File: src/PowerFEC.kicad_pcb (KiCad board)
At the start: 2 copper layers, 24 x 27.9 mm, 14 parts, among them J1 B2B-XH-A, P1 105444-0001, U1 AP22652

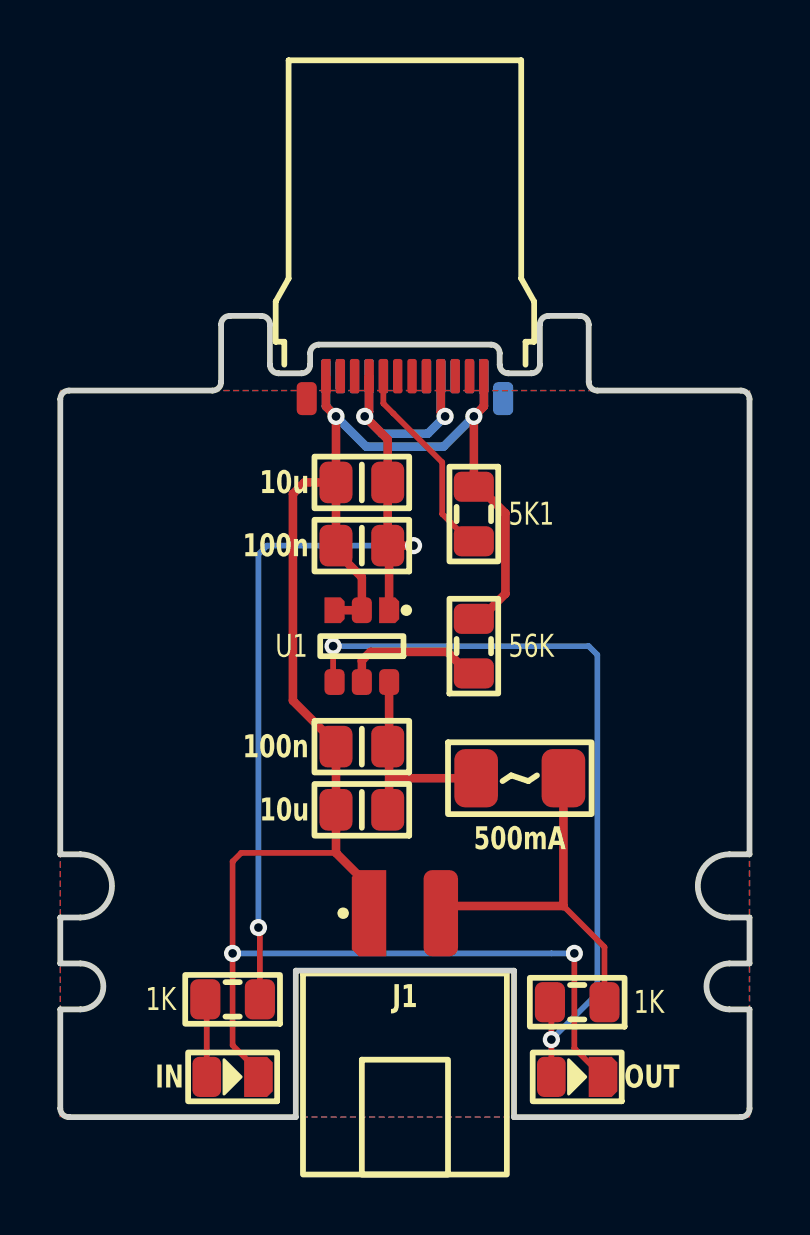
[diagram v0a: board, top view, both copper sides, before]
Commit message: Refactored to allow usage of PIC
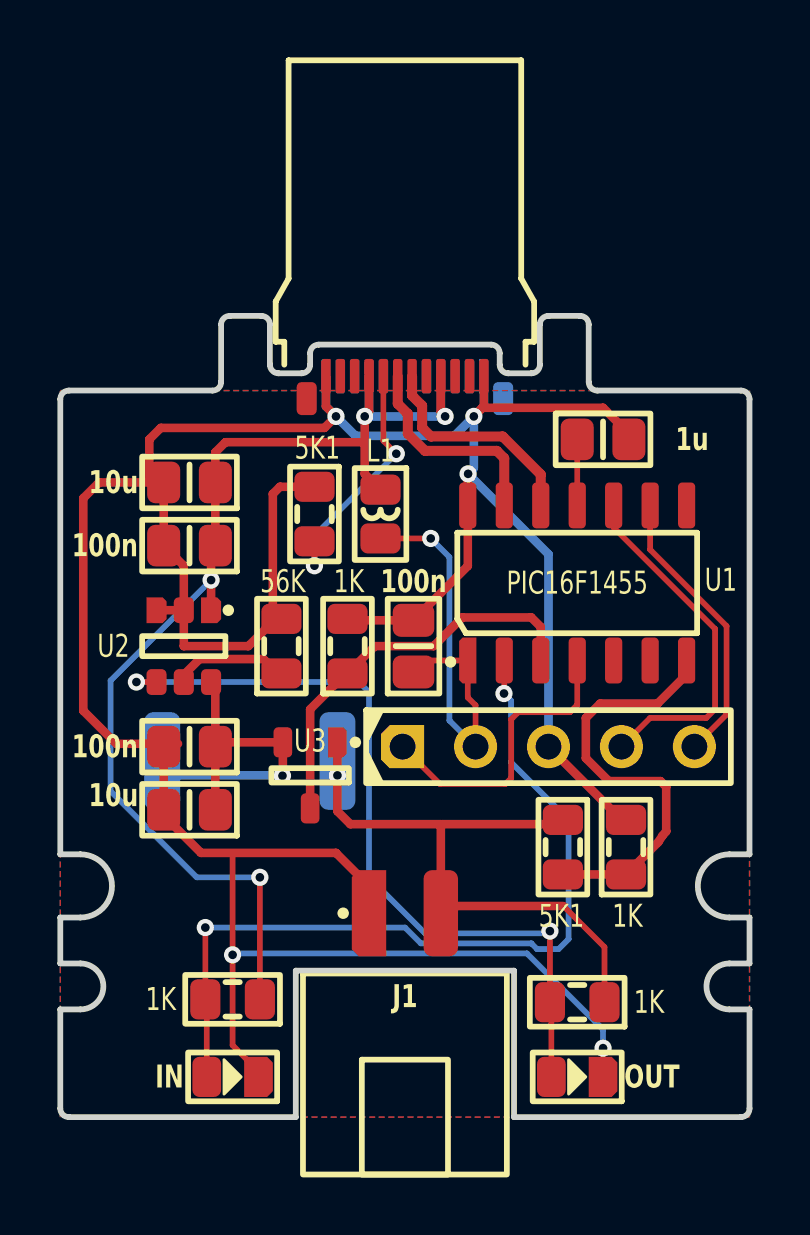
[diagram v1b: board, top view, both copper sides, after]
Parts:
- removed F?: 500mA, Medo64:F (1206)
- added C3: 100n, Medo64:C (0805), F.Cu at (32.3, 31.5)
- added C4: 1u, Medo64:C (0805), F.Cu at (38.9, 24.3)
- added ICSP: Microchip PIC, Medo64:ICSP PIC Pogo (5w), F.Cu at (37.0, 35.0)
- added L1: 1u, Medo64:L (0805), F.Cu at (31.1, 26.9)
- added R1: 0R1, Medo64:R (2512), B.Cu at (26.6, 35.5)
- added R2: 1K, Medo64:R (0805), F.Cu at (30.0, 31.5)
- added R4: 1K, Medo64:R (0805), F.Cu at (39.7, 38.5)
- added R5: 5K1, Medo64:R (0805), F.Cu at (37.5, 38.5)
- added U1: PIC16F1455, Medo64:U Micro PIC16F1455 (SOIC-14), F.Cu at (38.0, 29.3)
- added U3: ZXCT1009, Medo64:U CurrentSense ZXCT1009 (SOT23-3), F.Cu at (28.7, 36.0)
- moved R7 6.70 mm to (27.7, 31.5)
- moved U2 6.20 mm to (24.3, 31.5)
- moved C1 6.00 mm to (24.5, 28.0)
- moved C2 6.00 mm to (24.5, 35.0)
- moved C5 6.00 mm to (24.5, 25.8)
- moved C6 6.00 mm to (24.5, 37.2)
- moved R6 5.55 mm to (28.9, 26.9)
- renumbered C3 to C5, C4 to C6, R1 to R3, R2 to R4, R3 to R6, R4 to R7, U1 to U2
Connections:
- net FAULT# renamed LED_OUT
- net USB_Vin renamed Vin
- C2 pad 1: Vout -> Vsw
- C6 pad 1: Vout -> Vsw
- J1 pad 2: Vfused -> Vout
- R4 pad 1: Vfused -> Vout
- U2 pad 6: Vout -> Vsw
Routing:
- net GND: track 73.7 -> 117.9 mm, vias 4 -> 5
- net LED_IN: track 2.72 -> 28.9 mm, vias 0 -> 2
- net Vout: track 7.54 -> 22.7 mm, vias 0 -> 1
- net Vadc: track 0.00 -> 14.6 mm
- net 5V: track 0.00 -> 14.4 mm, vias 0 -> 1
- net Iadc: track 0.00 -> 14.1 mm
- net Vfused: track 12.9 -> 0.00 mm
- net ICSP_DAT: track 0.00 -> 12.4 mm
- net Vsw: track 0.00 -> 11.9 mm, vias 0 -> 1
- net ICSP_VPP: track 0.00 -> 10.5 mm
- net ICSP_CLK: track 0.00 -> 9.97 mm
- net USB_DM: track 0.00 -> 7.82 mm
- net USB_DP: track 0.00 -> 7.50 mm
- net Vin: track 38.3 -> 43.2 mm
- net V33: track 0.00 -> 2.30 mm
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
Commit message: Refactoring copper pours
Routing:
- net GND: track 117.9 -> 136.0 mm, vias 5 -> 6
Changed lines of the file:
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@@
   (segment (start 29.2 23.9) (end 23.5 23.9) (width 0.3) (layer "F.Cu") (net 4))
   (via (at 26 42.25) (size 0.6) (drill 0.3) (layers "F.Cu" "B.Cu") (net 4))
+  (via (at 35.5 39.1) (size 0.6) (drill 0.3) (layers "F.Cu" "B.Cu") (net 4))
   (via (at 34.2 25.5) (size 0.6) (drill 0.3) (layers "F.Cu" "B.Cu") (net 4))
   (via (at 29.6 23.5) (size 0.6) (drill 0.3) (layers "F.Cu" "B.Cu") (net 4))
@@
   (via (at 38.9 45.499992) (size 0.6) (drill 0.3) (layers "F.Cu" "B.Cu") (net 4))
   (segment (start 38.9 45.499992) (end 38.9 44.85) (width 0.2) (layer "B.Cu") (net 4))
+  (segment (start 34.2 25.5) (end 32.8 25.5) (width 0.3) (layer "B.Cu") (net 4))
   (segment (start 36.25 42.2) (end 26.05 42.2) (width 0.2) (layer "B.Cu") (net 4))
   (segment (start 26.05 42.2) (end 26 42.25) (width 0.2) (layer "B.Cu") (net 4))
+  (segment (start 33.2 34.2) (end 33.2 36.8) (width 0.3) (layer "B.Cu") (net 4))
   (segment (start 34.4 23.5) (end 34.4 25.3) (width 0.3) (layer "B.Cu") (net 4))
   (segment (start 34.75 23.15) (end 34.4 23.5) (width 0.3) (layer "B.Cu") (net 4))
+  (segment (start 32.8 25.5) (end 30.4 27.9) (width 0.3) (layer "B.Cu") (net 4))
   (segment (start 34.4 25.3) (end 34.2 25.5) (width 0.3) (layer "B.Cu") (net 4))
   (segment (start 29.25 23.15) (end 29.6 23.5) (width 0.3) (layer "B.Cu") (net 4))
@@
   (segment (start 33.724265 24.175735) (end 34.4 23.5) (width 0.3) (layer "B.Cu") (net 4))
   (segment (start 29.25 22.1) (end 29.25 23.15) (width 0.3) (layer "B.Cu") (net 4))
+  (segment (start 30.4 27.9) (end 30.4 31.4) (width 0.3) (layer "B.Cu") (net 4))
+  (segment (start 33.2 36.8) (end 35.5 39.1) (width 0.3) (layer "B.Cu") (net 4))
   (segment (start 29.6 23.5) (end 30.275735 24.175735) (width 0.3) (layer "B.Cu") (net 4))
   (segment (start 37 28.3) (end 34.2 25.5) (width 0.3) (layer "B.Cu") (net 4))
+  (segment (start 30.4 31.4) (end 33.2 34.2) (width 0.3) (layer "B.Cu") (net 4))
   (segment (start 30.1 37.7) (end 29.65 37.25) (width 0.3) (layer "F.Cu") (net 5))
   (segment (start 33.25 40.8) (end 33.25 37.7) (width 0.3) (layer "F.Cu") (net 5))
@@
   (segment (start 31.15 27.75) (end 32.9 27.75) (width 0.2) (layer "F.Cu") (net 8))
   (via (at 32.9 27.75) (size 0.6) (drill 0.3) (layers "F.Cu" "B.Cu") (net 8))
-  (segment (start 33.55 34.09) (end 34.46 35) (width 0.2) (layer "B.Cu") (net 8))
+  (segment (start 34.46 33.56) (end 34.46 35) (width 0.2) (layer "B.Cu") (net 8))
   (segment (start 32.9 27.75) (end 33.55 28.4) (width 0.2) (layer "B.Cu") (net 8))
-  (segment (start 33.55 28.4) (end 33.55 34.09) (width 0.2) (layer "B.Cu") (net 8))
+  (segment (start 33.55 28.4) (end 33.55 32.65) (width 0.2) (layer "B.Cu") (net 8))
+  (segment (start 33.55 32.65) (end 34.46 33.56) (width 0.2) (layer "B.Cu") (net 8))
   (segment (start 38 33.55) (end 38 32) (width 0.2) (layer "F.Cu") (net 9))
   (segment (start 35.7 36.1) (end 35.7 34.05) (width 0.2) (layer "F.Cu") (net 9))
@@
   (segment (start 27.722182 36) (end 23.55 36) (width 0.3) (layer "B.Cu") (net 17))
   (zone (net 4) (net_name "GND") (layers "F&B.Cu") (hatch edge 0.5)
-    (connect_pads (clearance 0.25))
-    (min_thickness 0.25) (filled_areas_thickness no)
+    (connect_pads no (clearance 0.3))
+    (min_thickness 0.3) (filled_areas_thickness no)
     (fill yes (thermal_gap 0.5) (thermal_bridge_width 0.5))
     (polygon

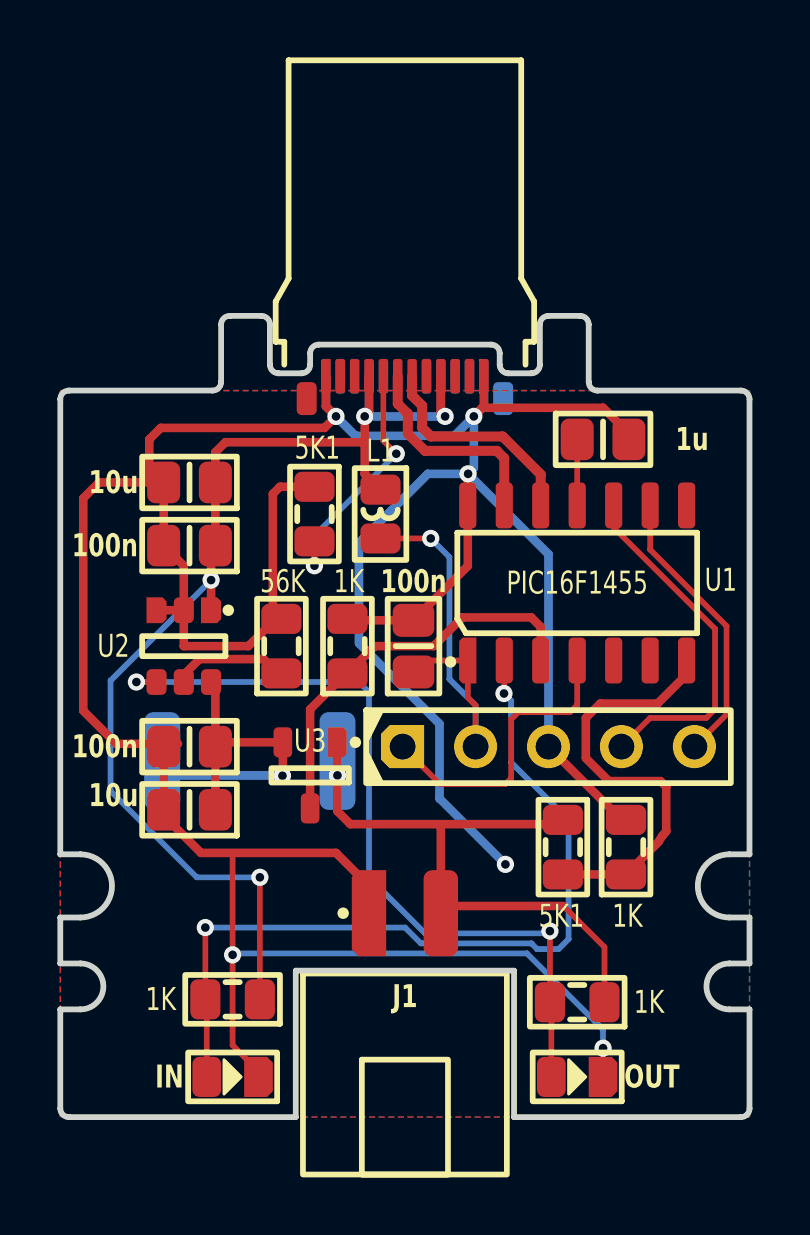
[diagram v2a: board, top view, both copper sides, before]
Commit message: Minor trace movements
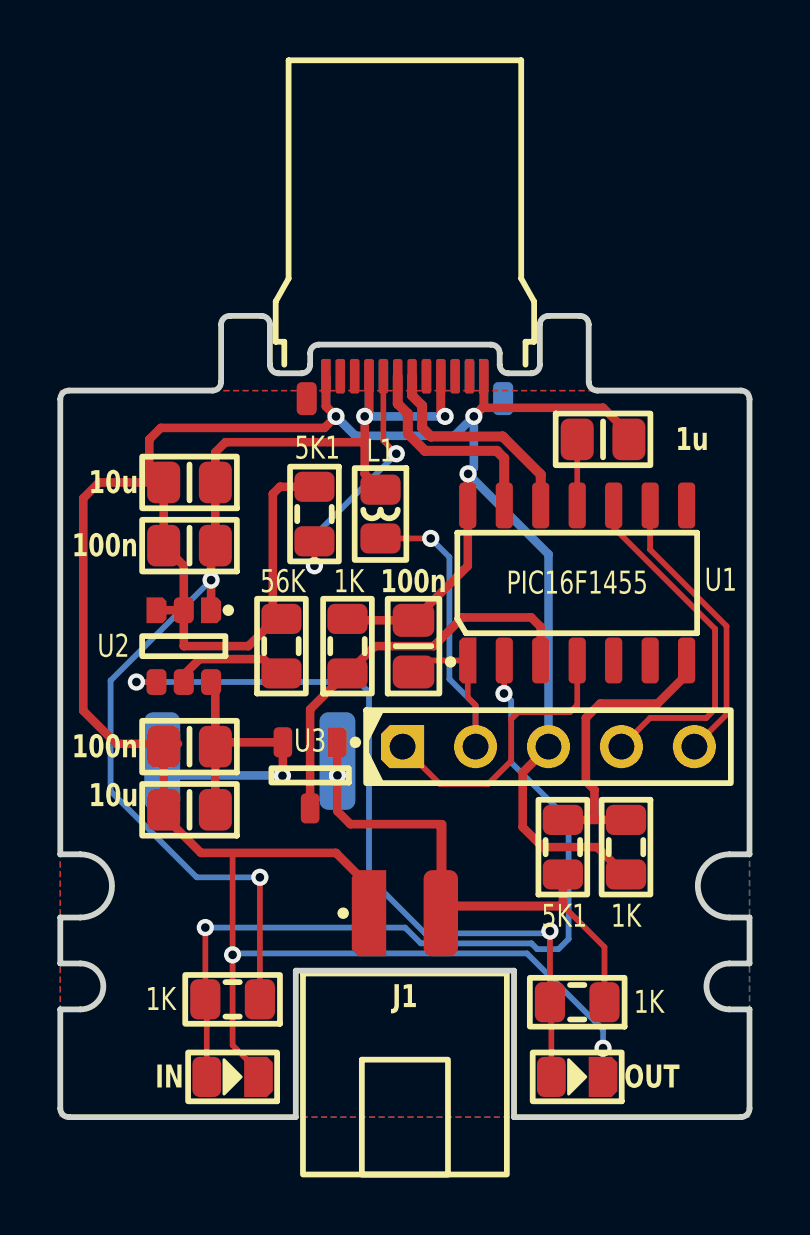
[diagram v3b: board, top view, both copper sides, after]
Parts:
- turned R4 to -90 degrees
- turned R5 to 90 degrees
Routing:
- net GND: track 136.0 -> 121.7 mm, vias 6 -> 5
- net Vadc: track 14.6 -> 10.0 mm
- net Vout: track 22.7 -> 26.8 mm

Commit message: Added soldermask expand
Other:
- rule pad_to_mask_clearance: 0 -> 0.05
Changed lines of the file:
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@@
       (dielectric_constraints no)
     )
-    (pad_to_mask_clearance 0)
+    (pad_to_mask_clearance 0.05)
     (aux_axis_origin 20 20)
     (pcbplotparams

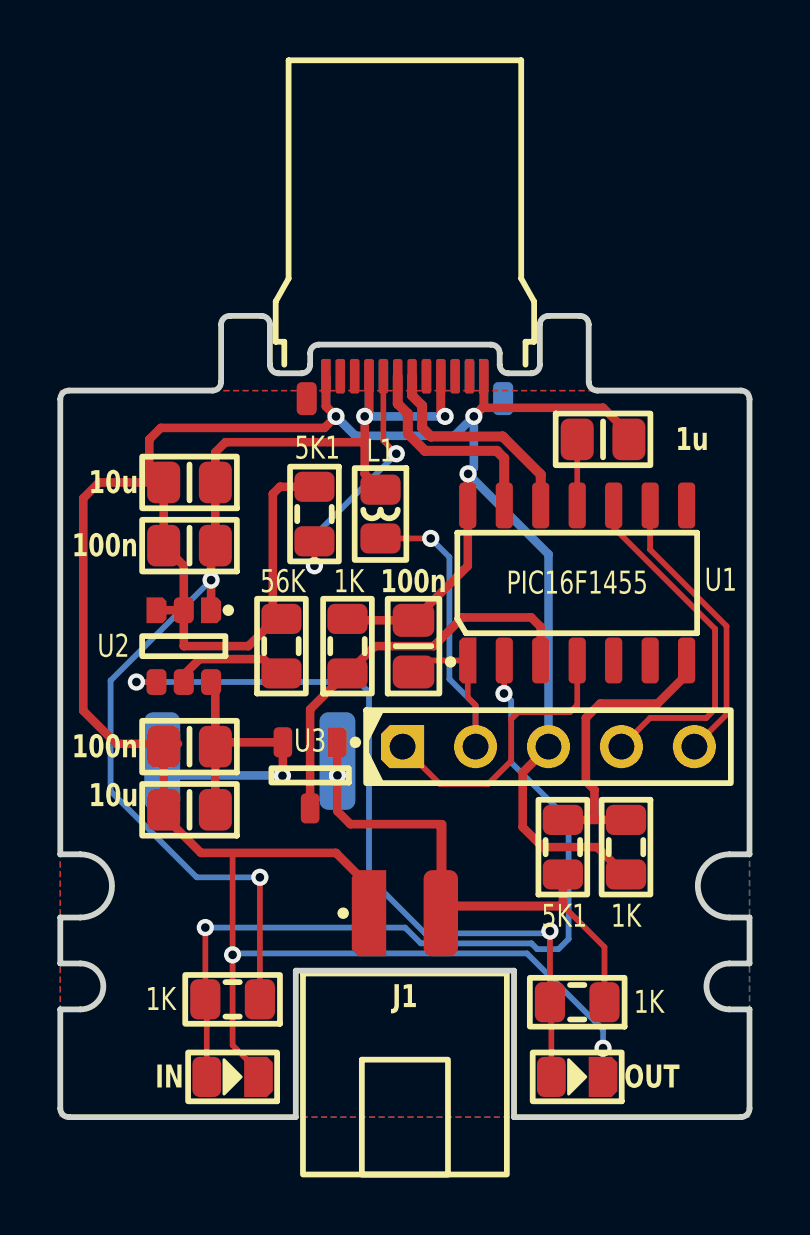
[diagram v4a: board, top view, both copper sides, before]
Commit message: Moved LEDs
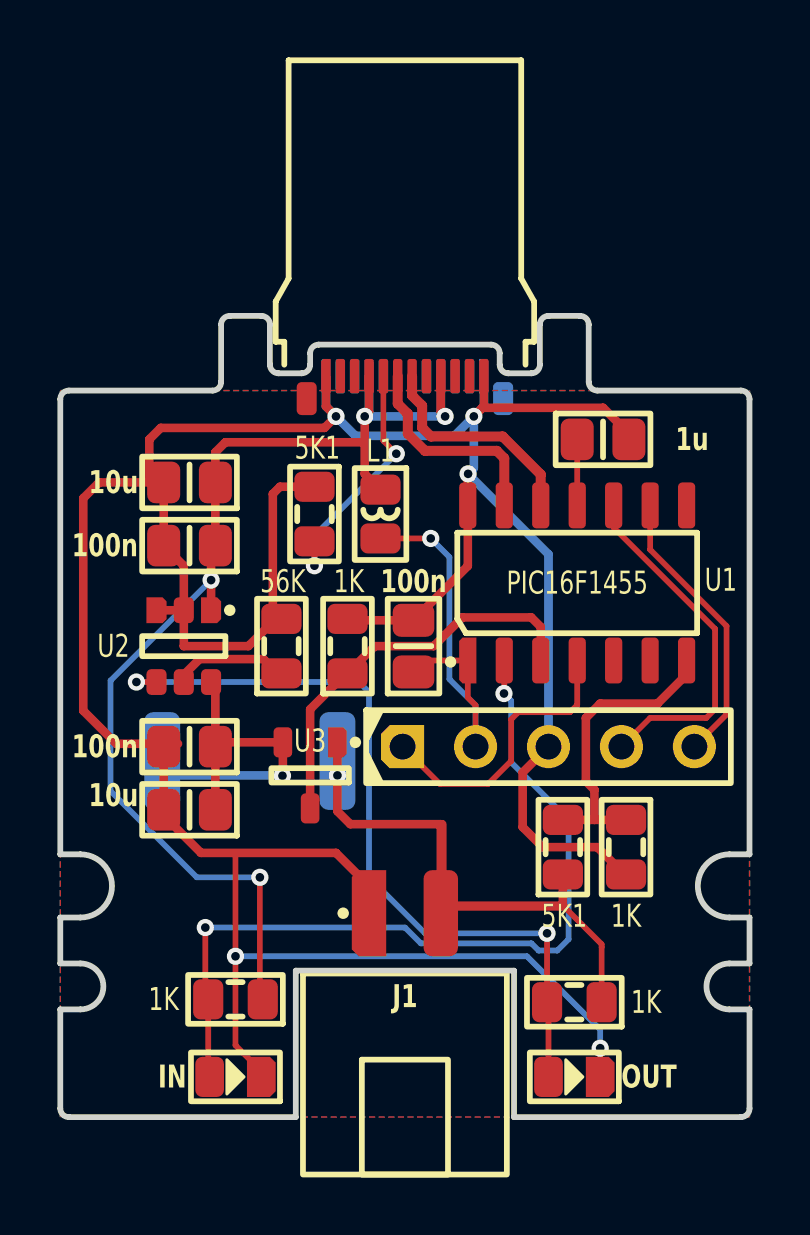
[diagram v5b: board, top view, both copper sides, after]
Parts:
- moved DS1 0.10 mm to (26.1, 46.5)
- moved DS2 0.10 mm to (37.9, 46.5)
- moved R3 0.10 mm to (26.1, 43.8)
- moved R4 0.10 mm to (37.9, 43.9)
